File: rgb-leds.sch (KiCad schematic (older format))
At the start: 602 parts

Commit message: zone movement + routing of all circuits
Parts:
- removed CON_LEDS?: CONN_01X04, Connectors_JST:JST_GH_BM04B-GHS-TBT_04x1.25mm_Straight, symbol CONN_01X04
- TP-LED-CKI1: renamed from TP-LED-CKI; footprint (none) -> Measurement_Points:Measurement_Point_Round-SMD-Pad_Small
- TP-LED-SDI1: renamed from TP-LED-SDI; footprint (none) -> Measurement_Points:Measurement_Point_Round-SMD-Pad_Small
- gave numbers to parts that had none: 599
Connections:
- wire segments 2521 -> 2518

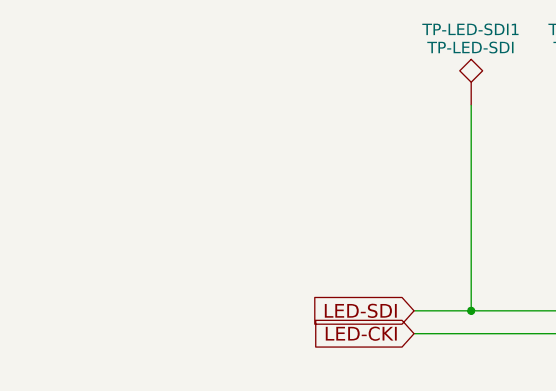
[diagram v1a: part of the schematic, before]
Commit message: splitting led power out from 5v so that we can insert the mosfet
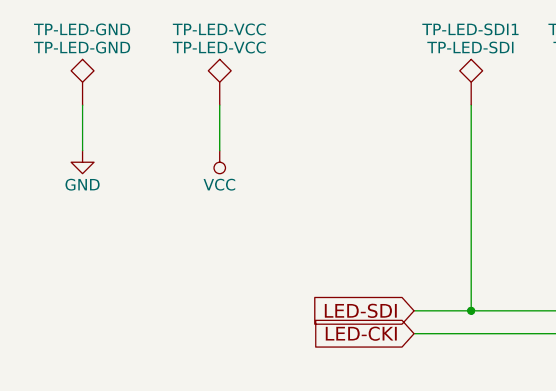
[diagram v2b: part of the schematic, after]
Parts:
- added TP-LED-GND: TP-LED-GND, Measurement_Points:Measurement_Point_Round-SMD-Pad_Small, symbol TEST
- added TP-LED-VCC: TP-LED-VCC, Measurement_Points:Measurement_Point_Round-SMD-Pad_Small, symbol TEST
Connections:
- net GND: now also TP-LED-GND.1
- net VCC: now also TP-LED-VCC.1

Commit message: Footprint updates
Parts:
- added JMP-LED-PWR-BYP: JMP-LED-PWR-BYP, Connect:GS2, symbol GS2
- added JMP-LED-PWR-EN-BYP: JMP-LED-PWR-EN-BYP, Connect:GS2, symbol GS2
- added Q?: IRLB8721PBF, TO_SOT_Packages_SMD:SOT-223-3_TabPin2, symbol IRLB8721PBF
- added R?: 10k, Resistors_SMD:R_0603, symbol R
- added TP-LED-PWR-EN: TP-LED-PWR-EN, Measurement_Points:Measurement_Point_Round-SMD-Pad_Small, symbol TEST
- renumbered TP-LED-GND to TP-LED-GND1, TP-LED-VCC to TP-LED-VCC1
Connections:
- net GND: now also R?.2
- net VCC: now also JMP-LED-PWR-BYP.1 (G1), Q?.3 (S)
- new net +3V3: JMP-LED-PWR-EN-BYP.2 (G2)
- new net +5V: JMP-LED-PWR-BYP.2 (G2), Q?.2 (D)
- new net LED-POWER-ENABLE: JMP-LED-PWR-EN-BYP.1 (G1), Q?.1 (G), R?.1, TP-LED-PWR-EN.1

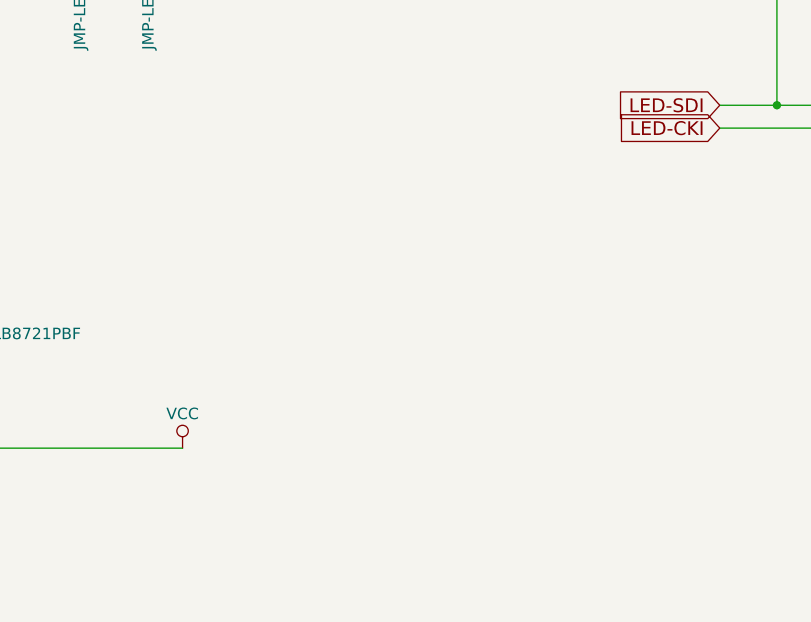
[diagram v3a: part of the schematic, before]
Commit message: Add leds for the three power planes
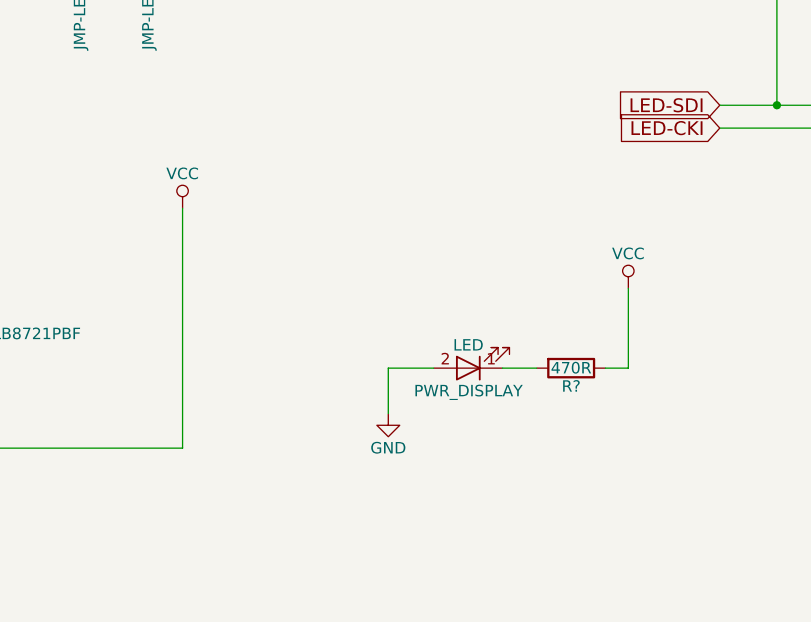
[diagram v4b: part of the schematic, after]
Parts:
- added PWR_DISPLAY: LED, LEDs:LED_0603, symbol LED
- added R?: 470R, Resistors_SMD:R_0603, symbol R
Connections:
- net GND: now also PWR_DISPLAY.2 (A)
- net VCC: now also R?.1
- new net: PWR_DISPLAY.1 (K), R?.2
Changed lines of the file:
@@
 L VCC #PWR?
 U 1 1 5B15BB43
-P -5950 850
-F 0 "#PWR?" H -5950 700 50  0001 C CNN
-F 1 "VCC" H -5950 1000 50  0000 C CNN
-F 2 "" H -5950 850 50  0001 C CNN
-F 3 "" H -5950 850 50  0001 C CNN
-	1    -5950 850
+P -5950 -200
+F 0 "#PWR?" H -5950 -350 50  0001 C CNN
+F 1 "VCC" H -5950 -50 50  0000 C CNN
+F 2 "" H -5950 -200 50  0001 C CNN
+F 3 "" H -5950 -200 50  0001 C CNN
+	1    -5950 -200
 	1    0    0    -1
 $EndComp
@@
 Wire Wire Line
 	-7000 150  -7000 -200
+Wire Wire Line
+	-5950 850  -5950 -200
+$Comp
+L R R?
+U 1 1 5B175334
+P -4250 500
+F 0 "R?" V -4170 500 50  0000 C CNN
+F 1 "470R" V -4250 500 50  0000 C CNN
+F 2 "Resistors_SMD:R_0603" V -4320 500 50  0001 C CNN
+F 3 "" H -4250 500 50  0001 C CNN
+	1    -4250 500
+	0    1    1    0
+$EndComp
+$Comp
+L GND #PWR?
+U 1 1 5B17533B
+P -5050 700
+F 0 "#PWR?" H -5050 450 50  0001 C CNN
+F 1 "GND" H -5050 550 50  0000 C CNN
+F 2 "" H -5050 700 50  0001 C CNN
+F 3 "" H -5050 700 50  0001 C CNN
+	1    -5050 700
+	1    0    0    -1
+$EndComp
+$Comp
+L LED PWR_DISPLAY
+U 1 1 5B175341
+P -4700 500
+F 0 "PWR_DISPLAY" H -4700 600 50  0000 C CNN
+F 1 "LED" H -4700 400 50  0000 C CNN
+F 2 "LEDs:LED_0603" H -4700 500 50  0001 C CNN
+F 3 "" H -4700 500 50  0001 C CNN
+	1    -4700 500
+	-1   0    0    1
+$EndComp
+Wire Wire Line
+	-4550 500  -4400 500
+Wire Wire Line
+	-4100 500  -4000 500
+Wire Wire Line
+	-5050 500  -5050 700
+Wire Wire Line
+	-4850 500  -5050 500
+Wire Wire Line
+	-4000 500  -4000 150
+$Comp
+L VCC #PWR?
+U 1 1 5B17665D
+P -4000 150
+F 0 "#PWR?" H -4000 0   50  0001 C CNN
+F 1 "VCC" H -4000 300 50  0000 C CNN
+F 2 "" H -4000 150 50  0001 C CNN
+F 3 "" H -4000 150 50  0001 C CNN
+	1    -4000 150
+	1    0    0    -1
+$EndComp
 $EndSCHEMATC

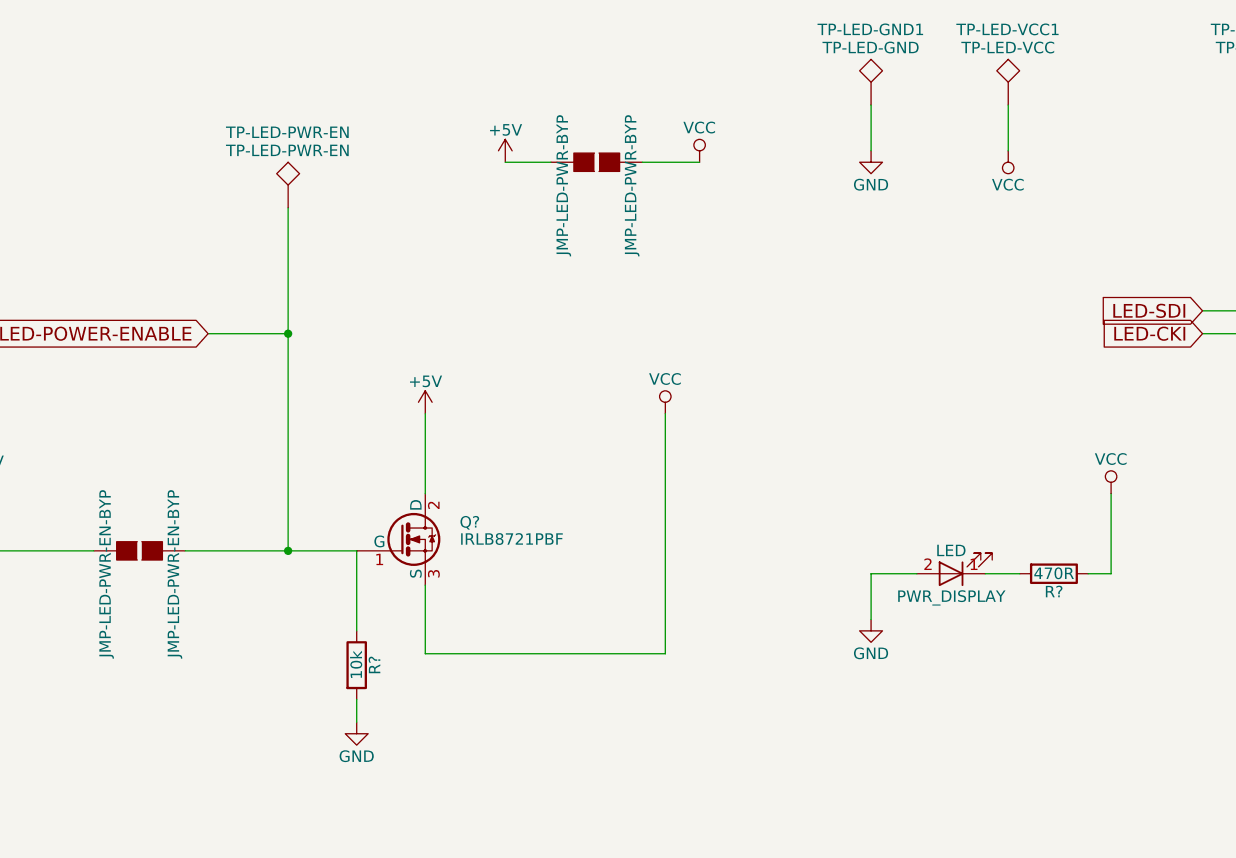
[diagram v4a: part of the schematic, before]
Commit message: Futher cleanup and footprint work, as well as power circuit fixes
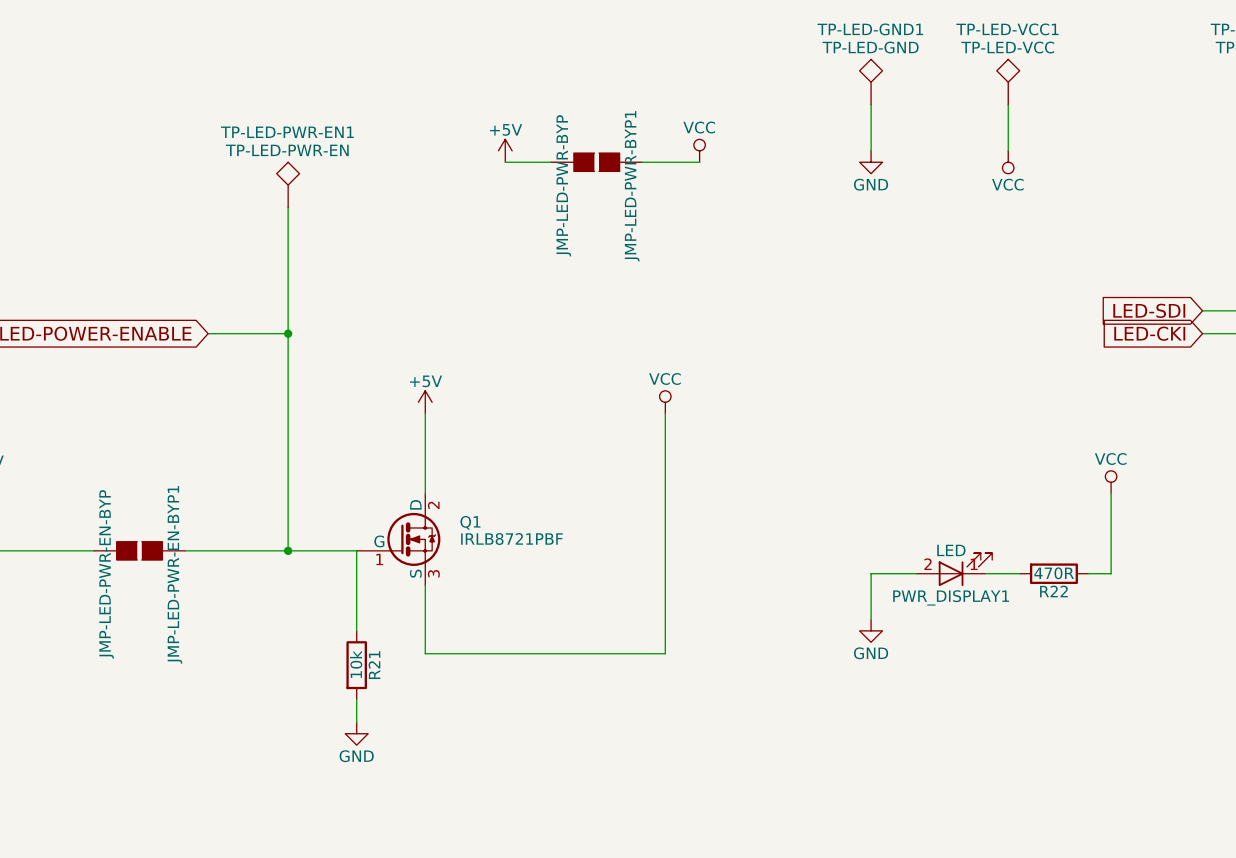
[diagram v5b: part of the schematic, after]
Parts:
- gave numbers to parts that had none: 3
- renumbered JMP-LED-PWR-BYP to JMP-LED-PWR-BYP1, JMP-LED-PWR-EN-BYP to JMP-LED-PWR-EN-BYP1, PWR_DISPLAY to PWR_DISPLAY1, TP-LED-PWR-EN to TP-LED-PWR-EN1

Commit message: Changing tp silkscreen names
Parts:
- removed C10, C11, C15, C16, C17, C18, C19, C2, C21, C23, C3, C5, C6, C7, C8: C_Small, Capacitors_SMD:C_0603, symbol C_Small
- C1, C12, C13, C14, C20, C22, C4, C9: value C_Small -> 1uF
- JMP-LED-PWR-BYP1: value JMP-LED-PWR-BYP -> LED-PWR
- JMP-LED-PWR-EN-BYP1: value JMP-LED-PWR-EN-BYP -> LED-EN
- TP-LED-CKI1: value TP-LED-CKI -> LED-CKI
- TP-LED-GND1: value TP-LED-GND -> LED-GND
- TP-LED-PWR-EN1: value TP-LED-PWR-EN -> LED-EN
- TP-LED-SDI1: value TP-LED-SDI -> LED-SDI
- TP-LED-VCC1: value TP-LED-VCC -> LED-VCC
